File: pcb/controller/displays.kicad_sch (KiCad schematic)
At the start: 0 parts

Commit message: retraced target pcb
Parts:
- added J4: 2.4 OLED, symbol Connector:Conn_01x04_Socket
- added J5: 0.96 OLED, symbol Connector:Conn_01x04_Socket
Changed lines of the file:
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@@
+		)
+	)
+	(symbol
+		(lib_id "Connector:Conn_01x04_Socket")
+		(at 121.92 53.34 0)
+		(unit 1)
+		(exclude_from_sim no)
+		(in_bom yes)
+		(on_board yes)
+		(dnp no)
+		(fields_autoplaced yes)
+		(property "Reference" "J5"
+			(at 123.19 53.3399 0)
+			(effects
+				(font
+					(size 1.27 1.27)
+				)
+				(justify left)
+			)
+		)
+		(property "Value" "0.96 OLED"
+			(at 123.19 55.8799 0)
+			(effects
+				(font
+					(size 1.27 1.27)
+				)
+				(justify left)
+			)
+		)
+		(property "Footprint" ""
+			(at 121.92 53.34 0)
+			(effects
+				(font
+					(size 1.27 1.27)
+				)
+				(hide yes)
+			)
+		)
+		(property "Datasheet" "~"
+			(at 121.92 53.34 0)
+			(effects
+				(font
+					(size 1.27 1.27)
+				)
+				(hide yes)
+			)
+		)
+		(property "Description" "Generic connector, single row, 01x04, script generated"
+			(at 121.92 53.34 0)
+			(effects
+				(font
+					(size 1.27 1.27)
+				)
+				(hide yes)
+			)
+		)
+		(pin "3"
+		)
+		(pin "4"
+		)
+		(pin "1"
+		)
+		(pin "2"
+		)
+		(instances
+			(project "controller"
+				(path "/c599d8cf-7937-49be-b4ed-eac09167ead4/674d50d3-0923-4cb8-9c9e-cea2437acbc8"
+					(reference "J5")
+					(unit 1)
+				)
+			)
+		)
+	)
+	(symbol
+		(lib_id "Connector:Conn_01x04_Socket")
+		(at 83.82 53.34 0)
+		(unit 1)
+		(exclude_from_sim no)
+		(in_bom yes)
+		(on_board yes)
+		(dnp no)
+		(fields_autoplaced yes)
+		(property "Reference" "J4"
+			(at 85.09 53.3399 0)
+			(effects
+				(font
+					(size 1.27 1.27)
+				)
+				(justify left)
+			)
+		)
+		(property "Value" "2.4 OLED"
+			(at 85.09 55.8799 0)
+			(effects
+				(font
+					(size 1.27 1.27)
+				)
+				(justify left)
+			)
+		)
+		(property "Footprint" ""
+			(at 83.82 53.34 0)
+			(effects
+				(font
+					(size 1.27 1.27)
+				)
+				(hide yes)
+			)
+		)
+		(property "Datasheet" "~"
+			(at 83.82 53.34 0)
+			(effects
+				(font
+					(size 1.27 1.27)
+				)
+				(hide yes)
+			)
+		)
+		(property "Description" "Generic connector, single row, 01x04, script generated"
+			(at 83.82 53.34 0)
+			(effects
+				(font
+					(size 1.27 1.27)
+				)
+				(hide yes)
+			)
+		)
+		(pin "3"
+		)
+		(pin "4"
+		)
+		(pin "1"
+		)
+		(pin "2"
+		)
+		(instances
+			(project ""
+				(path "/c599d8cf-7937-49be-b4ed-eac09167ead4/674d50d3-0923-4cb8-9c9e-cea2437acbc8"
+					(reference "J4")
+					(unit 1)
+				)
+			)
 		)
 	)

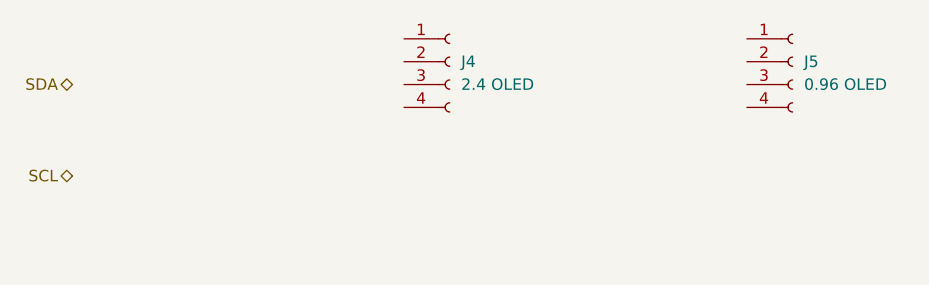
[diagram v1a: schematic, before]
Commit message: added lcsc numbers to all components and added ESD protection
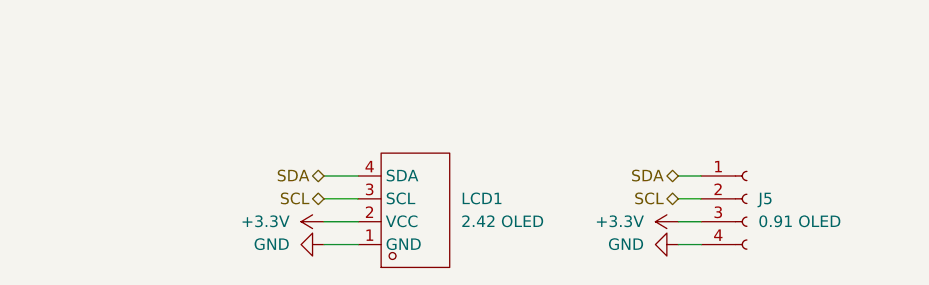
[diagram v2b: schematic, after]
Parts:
- removed J4: 2.4 OLED, symbol Connector:Conn_01x04_Socket
- added LCD1: 2.42 OLED, external_footprints.petty:LCD-TH_4P-L72.0-W43.0-P2.54_HS242L03W2C01, symbol custom:HS242L03W2C01
- J5: value 0.96 OLED -> 0.91 OLED; footprint (none) -> Connector_Wire:SolderWire-0.5sqmm_1x04_P4.6mm_D0.9mm_OD2.1mm; LCSC (none) -> C5248081
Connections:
- net SCL: now also J5.2 (Pin_2), LCD1.3 (SCL)
- net SDA: now also J5.1 (Pin_1), LCD1.4 (SDA)
- net +3.3V: now reaches J5.3 (Pin_3)
- net +3.3V: now also LCD1.2 (VCC)
- net GND: now reaches J5.4 (Pin_4)
- net GND: now also LCD1.1 (GND)
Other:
- moved on the sheet: J5
